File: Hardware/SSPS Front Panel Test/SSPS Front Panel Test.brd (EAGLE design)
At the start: 13.2 x 2.1 mm, 81 parts, among them J1 61400413321, SW1 B3W-9000-RG2C, SW2 B3W-9000-RG2C, U1 P8X32A-Q44, U10 STP16CP05XTTR, U11 FT230XS, U12 IP4234CZ6, U2 STP16CP05XTTR, U3 STP16CP05XTTR, U4 STP16CP05XTTR, U5 STP16CP05XTTR, U6 STP16CP05XTTR, U7 AP1084D25G-13, U8 AP1084D33G-13, U9 STP16CP05XTTR

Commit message: Test for Front Panel of SSPS complete.
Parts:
- removed DISP21: CU16025-UWJ6, PP_Displays:CU16025-UW6J
- removed H1, H2, H3, H4: MOUNT_HOLE150MIL, PP_Connectors:MOUNT_HOLE_150MIL
- added 5V: 5000, PP_Connectors:KEYSTONE_5115-5119
- added C17, C18, C19, C20, C21, C22, C23: .1uF, PP_Passives:0603
- added C24, C25, C26: 0.1uF, PP_Passives:0603
- added FID1, FID2: FIDUCIAL_100MIL, MF_Aesthetics:FIDUCIAL_100MIL
- added FRAME1: MF_FRAMEDEFAULT, MF_Aesthetics:MF_FRAME_DEFAULT
- added GND: 5001, PP_Connectors:KEYSTONE_5115-5119
- added J2: (no value), PP_Connectors:2.54MM_01X08_PIN_HEADER
- added LCD1: CU16025-UW6J, PP_Displays:CU16025-UW6J
- added R12, R13, R14, R16, R17, R18, R19, R20, R21, R22: 10K, PP_Passives:0603
- added R15: 1K, PP_Passives:0603
- added SW3: 5501, PP_Electromechanical:5501
- added U13: FT234XD-R, PP_DigitalIC:FT234X_DFN-12
- added U14: STP16CP05XTTR, PP_DigitalIC:STP16CP05XTTR_TTSOP-24
- added X1: ABMM-6.000MHZ-B2-T, MF_Frequency_Control:7MMX5MM
- U1: value P8X32A-Q44 -> P8X32A-M44; device MF_IC_Digital:LQFP44 -> PP_DigitalIC:P8X32A_QFN-44
- U11: value FT230XS -> CAT24C512WI-GT3; device MF_IC_Digital:SSOP16 -> PP_DigitalIC:SOIC-8_W
- moved EN1 279.4 mm to (102.2, 74.7), turned to 270 degrees
- moved SW2 207.7 mm to (125.5, 62.7)
- moved SW1 191.8 mm to (125.5, 79.8)
- moved U1 171.6 mm to (138.7, 47.0), flipped to the top
- moved C5 112.2 mm to (111.0, 12.8)
- moved D20 112.2 mm to (76.2, 36.8)
- moved D25 112.2 mm to (94.5, 36.8)
- moved C2 112.2 mm to (126.5, 27.1)
- moved C1 112.2 mm to (94.3, 25.8)
- moved C10 112.2 mm to (89.7, 51.1)
- moved C11 112.2 mm to (34.0, 51.1)
- moved C4 112.2 mm to (126.4, 12.9)
- moved C6 112.2 mm to (74.3, 25.9)
- moved C7 112.2 mm to (54.3, 25.9)
- moved C8 112.2 mm to (34.3, 25.9)
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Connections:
- removed net RX_LED: U11.14
- removed net TX_LED: U11.15
- removed net VDD: U1.18, U1.30, U1.40, U1.8
- removed net VSS: U1.17, U1.27, U1.39, U1.5
- new net DISP9_DATA: U14.P$22
- new net ENCODER_A: C25.1, R18.2, U1.4
- new net ENCODER_B: C26.1, R19.1, U1.3
- new net LCD_SCK: LCD1.P$19, U1.43
- new net LCD_SI/SO: LCD1.P$16, U1.41
- new net LCD_STB: LCD1.P$18, U1.42
- new net N$39: R15.2, U14.P$23
- new net N$40: EN1.1, U14.P$5
- new net N$41: EN1.2, U14.P$6
- new net N$42: EN1.4, U14.P$7
- new net N$43: SW1.CATHODE_1, U14.P$8
- new net N$44: SW1.CATHODE_2, U14.P$9
- new net N$45: SW2.CATHODE_1, U14.P$10
- new net N$46: SW2.CATHODE_2, U14.P$11
- new net N$47: SW3.CATHODE_1, U14.P$12
- new net N$48: SW3.CATHODE_2, U14.P$13
- new net N$49: R20.2, SW1.3
- new net N$50: R21.2, SW2.3
- new net N$54: R22.2, SW3.2
- new net P11: J2.1, U1.12
- new net P12: J2.2, U1.13
- new net P13: J2.3, U1.14
- new net P14: J2.4, U1.15
- new net P15: J2.5, U1.16
- new net P16: J2.6, U1.19
- new net P17: J2.7, U1.20
- new net P18: J2.8, U1.21
- new net P19: U1.22
- new net P20: U1.23
- new net P21: U1.24
- new net P22: U1.25
- new net P23: U1.26
- new net P24: U1.31
- new net P25: U1.32
- new net P26: U1.33
- new net P27: U1.34
- new net RES: C21.1, R14.1, U1.7
- new net SCL: R12.1, U1.35, U11.6
- new net SDA: R13.1, U1.36, U11.5
- new net SW_1: SW1.4, U1.9
- new net SW_2: SW2.4, U1.10
- new net SW_3: SW3.3, U1.11
- new net TERMINAL_A: EN1.A, R16.1, R18.1
- new net TERMINAL_B: EN1.B, R17.1, R19.2
- new net USB_RST: C21.2
- new net X0: U1.29, X1.P$3
- new net X1: U1.28, X1.P$1
- net 2.5V: now also EN1.5, SW1.ANODE_1, SW1.ANODE_2, SW2.ANODE_1, SW2.ANODE_2, SW3.ANODE_1, SW3.ANODE_2
- net 3.3V: now also C17.2, C18.2, C19.2, C20.2, C22.2, C23.2, C24.1, R12.2, R13.2, R14.2, R16.2, R17.2, R20.1, R21.1, R22.1, U1.18, U1.30, U1.40, U1.8, U11.8, U13.4, U14.P$24; no longer U11.12
- net 3V3OUT: now also U13.2, U13.3, U13.9; no longer U11.10, U11.11, U11.3
- net DISP1_DATA: now also U1.2
- net DISP8_DATA: now also U14.P$2
- net DISPX_CLK: now also U1.44, U14.P$3
- net DISPX_LAT: now also U1.1, U14.P$4
- net GND: now also C17.1, C18.1, C19.1, C20.1, C22.1, C23.1, C24.2, C25.2, C26.2, EN1.C, GND.P$1, LCD1.P$17, R15.1, SW1.1, SW2.1, SW3.1A, U1.17, U1.27, U1.39, U1.5, U1.6, U11.1, U11.2, U11.3, U11.4, U11.7, U13.5, U13.P$1, U14.P$1, U14.P$21, U14.PAD, X1.P$2, X1.P$4; no longer U11.13, U11.5
- net N$34: now also U13.1; no longer U11.9
- net N$36: now also U13.12; no longer U11.8
- net RX: now also U1.37, U13.10; no longer U11.4
- net TX: now also U1.38, U13.7; no longer U11.1
- net USB_!RST: now also U13.8; no longer U11.2
- net VBUS_SENSE: now also U13.6; no longer U11.16
- net VIN: now also 5V.P$1, LCD1.P$15
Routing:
- net 3.3V: track 249.9 -> 554.8 mm, vias 9 -> 20
- net VIN: track 30.6 -> 251.7 mm
- net LCD_SI/SO: track 0.00 -> 118.7 mm
- net ENCODER_B: track 0.00 -> 115.4 mm
- net LCD_STB: track 0.00 -> 112.6 mm
- net LCD_SCK: track 0.00 -> 109.0 mm
- net ENCODER_A: track 0.00 -> 105.4 mm
- net 2.5V: track 272.3 -> 371.1 mm
- net GND: track 428.9 -> 502.4 mm, vias 47 -> 60
- net N$47: track 0.00 -> 63.8 mm
- net N$43: track 0.00 -> 60.6 mm
- net DISP1_DATA: track 0.00 -> 57.8 mm, vias 0 -> 3
- net N$48: track 0.00 -> 55.5 mm
- net DISPX_CLK: track 216.7 -> 267.5 mm, vias 9 -> 12
- net SW_1: track 0.00 -> 49.3 mm, vias 0 -> 1
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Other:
- board size 13.2 x 2.1 mm -> 158.5 x 96.5 mm

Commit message: Fixed part numbers.
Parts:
- DISP2, DISP3, DISP4, DISP5: value PSA08-11GWA -> PSA08-11SRWA
- SW3: value 5501 -> 5501M112
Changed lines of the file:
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@@
 <elements>
 <element name="DISP1" library="PP_LED" package="PSA08-11SRWA" value="PSA08-11SRWA" x="94.346" y="15.78"/>
-<element name="DISP2" library="PP_LED" package="PSA08-11SRWA" value="PSA08-11GWA" x="74.346" y="15.78"/>
-<element name="DISP3" library="PP_LED" package="PSA08-11SRWA" value="PSA08-11GWA" x="54.346" y="15.78"/>
-<element name="DISP4" library="PP_LED" package="PSA08-11SRWA" value="PSA08-11GWA" x="34.346" y="15.78"/>
+<element name="DISP2" library="PP_LED" package="PSA08-11SRWA" value="PSA08-11SRWA" x="74.346" y="15.78"/>
+<element name="DISP3" library="PP_LED" package="PSA08-11SRWA" value="PSA08-11SRWA" x="54.346" y="15.78"/>
+<element name="DISP4" library="PP_LED" package="PSA08-11SRWA" value="PSA08-11SRWA" x="34.346" y="15.78"/>
 <element name="D1" library="PP_LED" package="WP1043" value="WP1043ID" x="6.896" y="36.78" rot="R180"/>
 <element name="D2" library="PP_LED" package="WP1043" value="WP1043ID" x="10.546" y="36.78" rot="R180"/>
@@
 <element name="D7" library="PP_LED" package="WP1043" value="WP1043YD" x="28.796" y="36.78" rot="R180"/>
 <element name="D8" library="PP_LED" package="WP1043" value="WP1043YD" x="32.446" y="36.78" rot="R180"/>
-<element name="DISP5" library="PP_LED" package="PSA08-11SRWA" value="PSA08-11GWA" x="14.346" y="15.78"/>
+<element name="DISP5" library="PP_LED" package="PSA08-11SRWA" value="PSA08-11SRWA" x="14.346" y="15.78"/>
 <element name="D9" library="PP_LED" package="WP1043" value="WP1043YD" x="36.096" y="36.78" rot="R180"/>
 <element name="D10" library="PP_LED" package="WP1043" value="WP1043YD" x="39.746" y="36.78" rot="R180"/>
@@
 <attribute name="NAME" x="152.4" y="20.32" size="0.8128" layer="25" font="vector" ratio="16"/>
 </element>
-<element name="SW3" library="PP_Electromechanical" package="5501" value="5501" x="141.478" y="24.13" rot="R90"/>
+<element name="SW3" library="PP_Electromechanical" package="5501" value="5501M112" x="141.478" y="24.13" rot="R90"/>
 <element name="U14" library="PP_DigitalIC" package="STP16CP05XTTR_TTSOP-24" value="STP16CP05XTTR" x="110.998" y="56.388" rot="MR180"/>
 <element name="C24" library="PP_Passives" package="0603" value="0.1uF" x="110.998" y="50.038" rot="MR0"/>

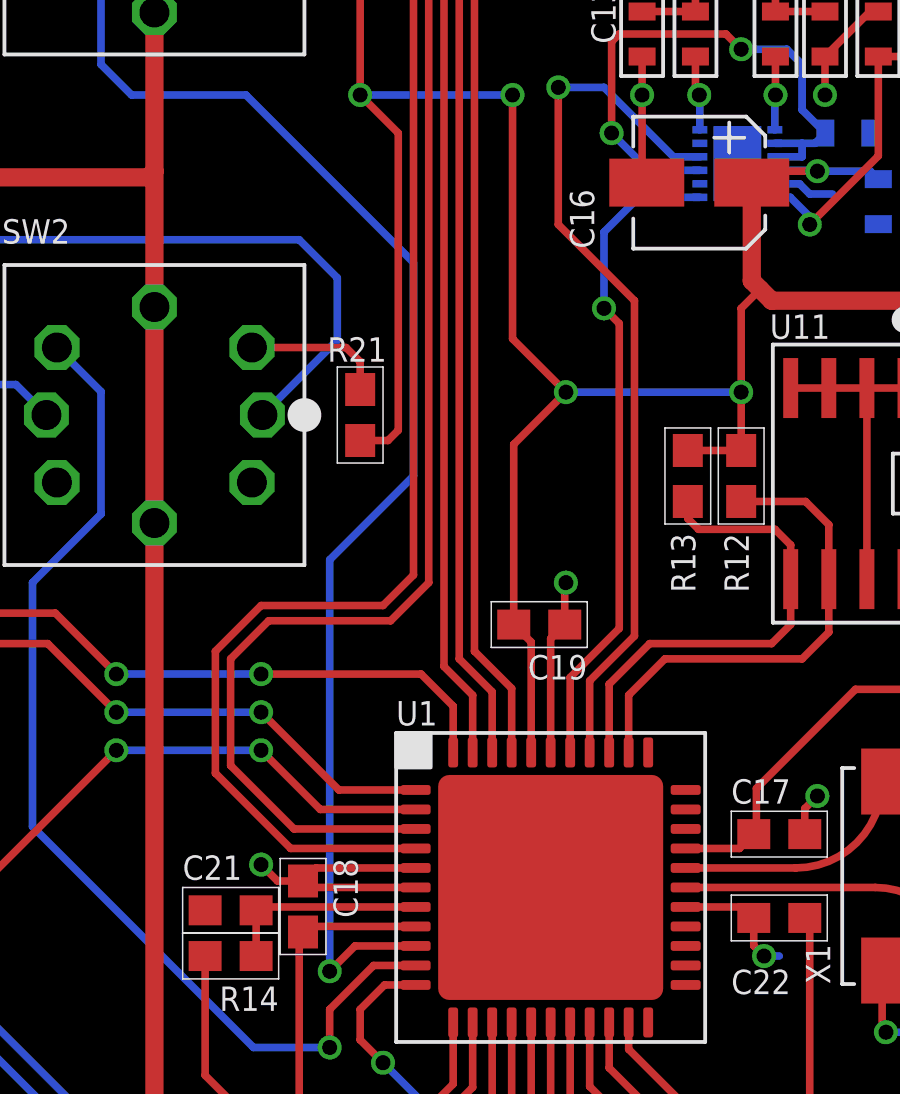
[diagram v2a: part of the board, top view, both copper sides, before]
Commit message: Fixed USB_!RST net...
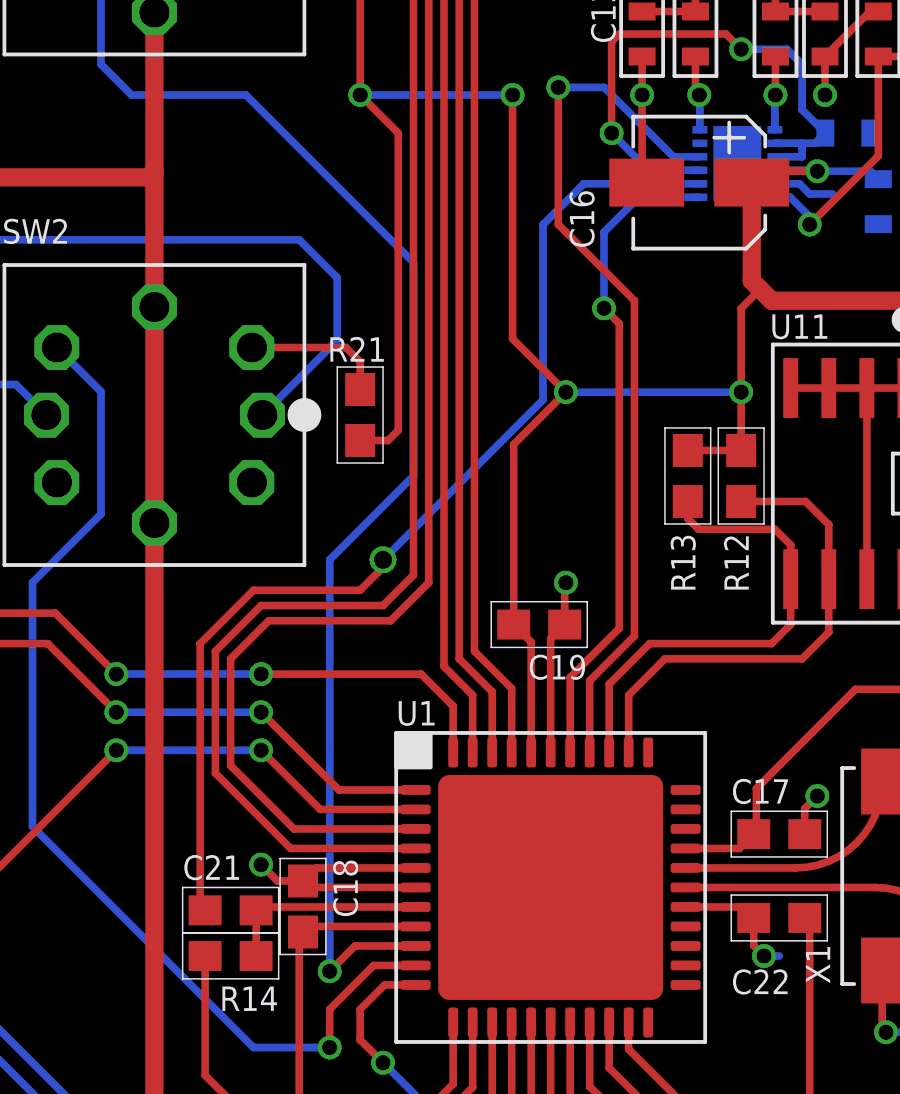
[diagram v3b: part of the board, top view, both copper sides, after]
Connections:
- removed net USB_RST: C21.2
- net USB_!RST: now also C21.2
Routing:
- net USB_!RST: track 0.00 -> 35.6 mm, vias 0 -> 1
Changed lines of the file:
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@@
 <signal name="USB_!RST">
 <contactref element="U13" pad="8"/>
+<contactref element="C21" pad="2"/>
+<wire x1="127.166" y1="46.228" x2="127" y2="46.228" width="0.254" layer="1"/>
+<wire x1="127" y1="46.228" x2="127" y2="55.118" width="0.254" layer="1"/>
+<wire x1="127" y1="55.118" x2="128.778" y2="56.896" width="0.254" layer="1"/>
+<wire x1="128.778" y1="56.896" x2="132.334" y2="56.896" width="0.254" layer="1"/>
+<wire x1="132.334" y1="56.896" x2="133.096" y2="57.658" width="0.254" layer="1"/>
+<wire x1="133.096" y1="57.658" x2="133.096" y2="57.912" width="0.254" layer="1"/>
+<via x="133.096" y="57.912" extent="1-16" drill="0.6" shape="square"/>
+<wire x1="133.096" y1="57.912" x2="138.43" y2="63.246" width="0.254" layer="16"/>
+<wire x1="138.43" y1="63.246" x2="138.43" y2="69.088" width="0.254" layer="16"/>
+<wire x1="138.43" y1="69.088" x2="139.787" y2="70.445" width="0.254" layer="16"/>
+<wire x1="139.787" y1="70.445" x2="143.657" y2="70.445" width="0.254" layer="16"/>
 </signal>
 <signal name="SDA">
@@
 <contactref element="U1" pad="33"/>
 </signal>
-<signal name="USB_RST">
-<contactref element="C21" pad="2"/>
-</signal>
 <signal name="LCD_SI/SO">
